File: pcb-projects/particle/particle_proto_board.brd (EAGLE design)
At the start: 94.6 x 65.7 mm, 35 parts, among them IC1 ATTINY20-MMH, IC2 DMC2400V, IC3 DMC2400V

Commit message: close 21, close 22
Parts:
- added SPI: 332-06, con-garry:332-06
- TPI: value 332-04 -> 332-06; device con-garry:332-04 -> con-garry:332-06
- moved TPI 84.6 mm to (-5.08, 6.35), turned to 0 degrees
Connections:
- removed net N$22: IC1.14, LED3.A, TP12.TP
- removed net N$23: IC1.15, LED2.A, TP11.TP
- removed net TPI_DATA: IC1.12, TPI.4
- new net MISO: IC1.14, LED3.A, SPI.1, TP12.TP
- new net SCK: IC1.15, LED2.A, SPI.3, TP11.TP
- new net TPI_DATA/MOSI: IC1.12, SPI.4, TPI.1
- net GND: now also SPI.6, TPI.4, TPI.6; no longer TPI.1
- net RESET: now also SPI.5, TPI.5; no longer TPI.3
- net TPI_CLK: now also TPI.3; no longer TPI.2
- net VCC: now also SPI.2, TPI.2
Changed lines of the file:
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@@
 </autorouter>
 <elements>
-<element name="TPI" library="con-garry" package="332-04" value="332-04" x="71.12" y="43.18" smashed="yes" rot="R90">
-<attribute name="NAME" x="70.835" y="37.75" size="1.27" layer="25" rot="R90"/>
-<attribute name="VALUE" x="67.58" y="41.56" size="1.27" layer="27" rot="R90"/>
-</element>
 <element name="IC1" library="tiny_particles_MCU" package="QFN45P300X300X85-21N" value="ATTINY20-MMH" x="63.1825" y="48.5775"/>
 <element name="R5" library="rcl" package="R1210" value="470" x="87.9475" y="56.1975"/>
@@
 <attribute name="TP_SIGNAL_NAME" value="" x="32.385" y="-16.8275" size="1.778" layer="27" display="off"/>
 </element>
+<element name="TPI" library="con-garry" package="332-06" value="332-06" x="-5.08" y="6.35"/>
+<element name="SPI" library="con-garry" package="332-06" value="332-06" x="-13.335" y="6.35"/>
 </elements>
 <signals>
 <signal name="GND">
-<contactref element="TPI" pad="1"/>
 <contactref element="IC1" pad="8"/>
 <contactref element="IC1" pad="21"/>
@@
 <contactref element="R6" pad="1"/>
 <contactref element="R9" pad="1"/>
-<wire x1="56.0675" y1="28.575" x2="56.9675" y2="4.23" width="0" layer="19" extent="1-1"/>
+<contactref element="TPI" pad="6"/>
+<contactref element="SPI" pad="6"/>
+<contactref element="TPI" pad="4"/>
+<wire x1="89.03" y1="52.07" x2="89.3475" y2="56.1975" width="0" layer="19" extent="1-1"/>
+<wire x1="89.03" y1="47.9425" x2="89.03" y2="52.07" width="0" layer="19" extent="1-1"/>
+<wire x1="63.1825" y1="48.5775" x2="89.03" y2="47.9425" width="0" layer="19" extent="1-1"/>
+<wire x1="63.1825" y1="47.1297" x2="63.1825" y2="48.5775" width="0" layer="19" extent="1-1"/>
+<wire x1="56.0675" y1="28.575" x2="63.1825" y2="47.1297" width="0" layer="19" extent="1-1"/>
 <wire x1="50.3525" y1="28.575" x2="56.0675" y2="28.575" width="0" layer="19" extent="1-1"/>
-<wire x1="3.68" y1="32.0675" x2="50.3525" y2="28.575" width="0" layer="19" extent="1-1"/>
-<wire x1="3.68" y1="45.4025" x2="3.68" y2="32.0675" width="0" layer="19" extent="1-1"/>
-<wire x1="36.6475" y1="54.0775" x2="3.68" y2="45.4025" width="0" layer="19" extent="1-1"/>
-<wire x1="63.1825" y1="47.1297" x2="36.6475" y2="54.0775" width="0" layer="19" extent="1-1"/>
-<wire x1="63.1825" y1="48.5775" x2="63.1825" y2="47.1297" width="0" layer="19" extent="1-1"/>
-<wire x1="72.12" y1="42.18" x2="63.1825" y2="47.1297" width="0" layer="19" extent="1-1"/>
-<wire x1="89.03" y1="47.9425" x2="72.12" y2="42.18" width="0" layer="19" extent="1-1"/>
-<wire x1="89.03" y1="52.07" x2="89.03" y2="47.9425" width="0" layer="19" extent="1-1"/>
-<wire x1="89.3475" y1="56.1975" x2="89.03" y2="52.07" width="0" layer="19" extent="1-1"/>
+<wire x1="56.9675" y1="4.23" x2="56.0675" y2="28.575" width="0" layer="19" extent="1-1"/>
+<wire x1="36.6475" y1="54.0775" x2="63.1825" y2="48.5775" width="0" layer="19" extent="1-1"/>
+<wire x1="3.68" y1="45.4025" x2="36.6475" y2="54.0775" width="0" layer="19" extent="1-1"/>
+<wire x1="3.68" y1="32.0675" x2="3.68" y2="45.4025" width="0" layer="19" extent="1-1"/>
+<wire x1="-3.08" y1="7.35" x2="3.68" y2="32.0675" width="0" layer="19" extent="1-1"/>
+<wire x1="-5.08" y1="7.35" x2="-3.08" y2="7.35" width="0" layer="19" extent="1-1"/>
+<wire x1="-11.335" y1="7.35" x2="-5.08" y2="7.35" width="0" layer="19" extent="1-1"/>
 </signal>
 <signal name="TPI_CLK">
-<contactref element="TPI" pad="2"/>
 <contactref element="IC1" pad="11"/>
-<wire x1="64.6303" y1="47.6885" x2="70.12" y2="42.18" width="0" layer="19" extent="1-1"/>
+<contactref element="TPI" pad="3"/>
+<wire x1="-5.08" y1="5.35" x2="64.6303" y2="47.6885" width="0" layer="19" extent="1-1"/>
 </signal>
 <signal name="PWR_TX_B">
@@
 <wire x1="61.7347" y1="48.1203" x2="37.1475" y2="54.0775" width="0" layer="19" extent="1-1"/>
 </signal>
-<signal name="TPI_DATA">
-<contactref element="TPI" pad="4"/>
+<signal name="TPI_DATA/MOSI">
 <contactref element="IC1" pad="12"/>
-<wire x1="64.6303" y1="48.1203" x2="70.12" y2="44.18" width="0" layer="19" extent="1-1"/>
+<contactref element="TPI" pad="1"/>
+<contactref element="SPI" pad="4"/>
+<wire x1="-7.08" y1="5.35" x2="64.6303" y2="48.1203" width="0" layer="19" extent="1-1"/>
+<wire x1="-13.335" y1="7.35" x2="-7.08" y2="5.35" width="0" layer="19" extent="1-1"/>
 </signal>
 <signal name="RESET">
-<contactref element="TPI" pad="3"/>
 <contactref element="IC1" pad="13"/>
-<wire x1="64.6303" y1="48.5775" x2="72.12" y2="44.18" width="0" layer="19" extent="1-1"/>
+<contactref element="TPI" pad="5"/>
+<contactref element="SPI" pad="5"/>
+<wire x1="-3.08" y1="5.35" x2="64.6303" y2="48.5775" width="0" layer="19" extent="1-1"/>
+<wire x1="-11.335" y1="5.35" x2="-3.08" y2="5.35" width="0" layer="19" extent="1-1"/>
 </signal>
 <signal name="RX_B" class="1">
@@
 <wire x1="64.0715" y1="50.0253" x2="71.4375" y2="54.9275" width="0" layer="19" extent="1-1"/>
 </signal>
-<signal name="N$22">
+<signal name="MISO">
 <contactref element="IC1" pad="14"/>
 <contactref element="LED3" pad="A"/>
 <contactref element="TP12" pad="TP"/>
+<contactref element="SPI" pad="1"/>
 <wire x1="71.12" y1="48.5775" x2="74.45" y2="49.2125" width="0" layer="19" extent="1-1"/>
 <wire x1="64.6303" y1="49.0347" x2="71.12" y2="48.5775" width="0" layer="19" extent="1-1"/>
-</signal>
-<signal name="N$23">
+<wire x1="-15.335" y1="5.35" x2="64.6303" y2="49.0347" width="0" layer="19" extent="1-1"/>
+</signal>
+<signal name="SCK">
 <contactref element="LED2" pad="A"/>
 <contactref element="TP11" pad="TP"/>
 <contactref element="IC1" pad="15"/>
+<contactref element="SPI" pad="3"/>
 <wire x1="71.4375" y1="51.7525" x2="74.45" y2="52.07" width="0" layer="19" extent="1-1"/>
 <wire x1="64.6303" y1="49.4665" x2="71.4375" y2="51.7525" width="0" layer="19" extent="1-1"/>
+<wire x1="-13.335" y1="5.35" x2="64.6303" y2="49.4665" width="0" layer="19" extent="1-1"/>
 </signal>
 <signal name="N$24">
@@
 <contactref element="IC3" pad="4"/>
 <contactref element="IC2" pad="4"/>
+<contactref element="TPI" pad="2"/>
+<contactref element="SPI" pad="2"/>
 <wire x1="47.4375" y1="28.575" x2="63.6397" y2="47.1297" width="0" layer="19" extent="1-1"/>
 <wire x1="57.9675" y1="5.93" x2="47.4375" y2="28.575" width="0" layer="19" extent="1-1"/>
 <wire x1="37.6475" y1="55.7775" x2="63.6397" y2="47.1297" width="0" layer="19" extent="1-1"/>
 <wire x1="17.275" y1="59.055" x2="37.6475" y2="55.7775" width="0" layer="19" extent="1-1"/>
+<wire x1="-7.08" y1="7.35" x2="17.275" y2="59.055" width="0" layer="19" extent="1-1"/>
+<wire x1="-15.335" y1="7.35" x2="-7.08" y2="7.35" width="0" layer="19" extent="1-1"/>
 </signal>
 <signal name="N$1">

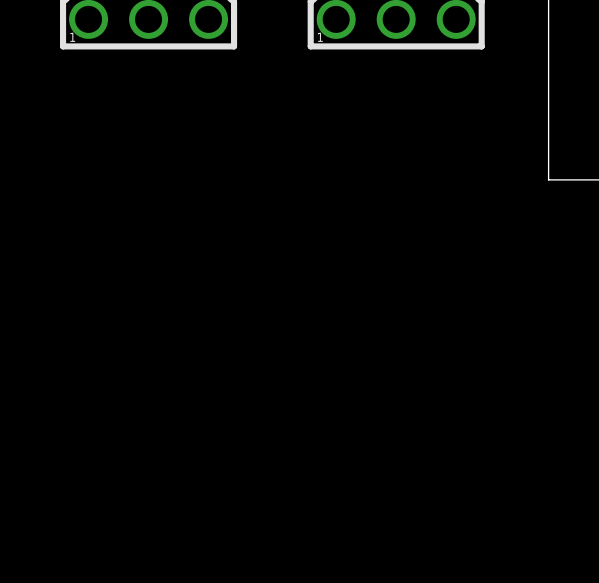
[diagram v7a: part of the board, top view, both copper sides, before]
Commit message: fixes #13
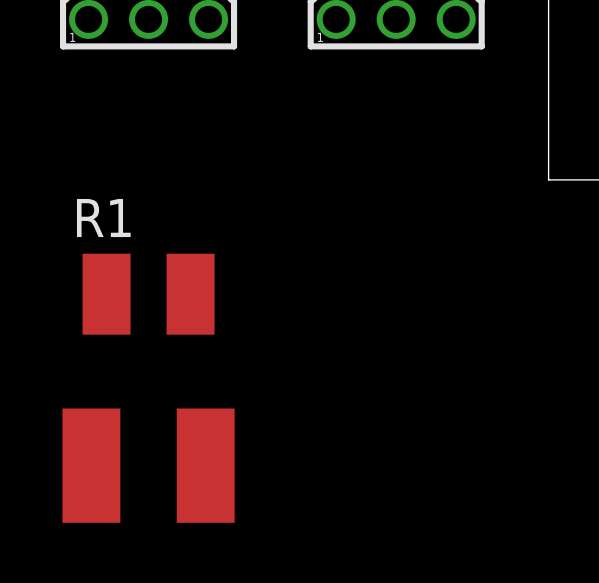
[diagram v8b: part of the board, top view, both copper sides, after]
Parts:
- added R1: 1k, rcl:R1210
- added RESET-SW: PAD-RESET-SWITCH, reset_pad:SWITCH-PAD-FORMED
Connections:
- net GND: now also RESET-SW.P$1
- net RESET: now also R1.1, RESET-SW.P$2
- net VCC: now also R1.2
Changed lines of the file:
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@@
 <layer number="54" name="bGND_GNDA" color="1" fill="9" visible="no" active="no"/>
 <layer number="56" name="wert" color="7" fill="1" visible="no" active="no"/>
+<layer number="90" name="Modules" color="5" fill="1" visible="no" active="no"/>
 <layer number="91" name="Nets" color="2" fill="1" visible="no" active="no"/>
 <layer number="92" name="Busses" color="1" fill="1" visible="no" active="no"/>
@@
 <element name="TPI" library="con-garry" package="332-06" value="332-06" x="-5.08" y="6.35"/>
 <element name="SPI" library="con-garry" package="332-06" value="332-06" x="-13.335" y="6.35"/>
+<element name="R1" library="rcl" package="R1210" value="1k" x="-13.335" y="-3.81"/>
+<element name="RESET-SW" library="reset_pad" package="SWITCH-PAD-FORMED" value="PAD-RESET-SWITCH" x="-13.97" y="-9.525"/>
 </elements>
 <signals>
@@
 <contactref element="SPI" pad="6"/>
 <contactref element="TPI" pad="4"/>
+<contactref element="RESET-SW" pad="P$1"/>
 <wire x1="89.03" y1="52.07" x2="89.3475" y2="56.1975" width="0" layer="19" extent="1-1"/>
 <wire x1="89.03" y1="47.9425" x2="89.03" y2="52.07" width="0" layer="19" extent="1-1"/>
@@
 <wire x1="-5.08" y1="7.35" x2="-3.08" y2="7.35" width="0" layer="19" extent="1-1"/>
 <wire x1="-11.335" y1="7.35" x2="-5.08" y2="7.35" width="0" layer="19" extent="1-1"/>
+<wire x1="-15.24" y1="-9.525" x2="-11.335" y2="7.35" width="0" layer="19" extent="1-1"/>
 </signal>
 <signal name="TPI_CLK">
@@
 <contactref element="TPI" pad="5"/>
 <contactref element="SPI" pad="5"/>
+<contactref element="R1" pad="1"/>
+<contactref element="RESET-SW" pad="P$2"/>
 <wire x1="-3.08" y1="5.35" x2="64.6303" y2="48.5775" width="0" layer="19" extent="1-1"/>
 <wire x1="-11.335" y1="5.35" x2="-3.08" y2="5.35" width="0" layer="19" extent="1-1"/>
+<wire x1="-14.735" y1="-3.81" x2="-11.335" y2="5.35" width="0" layer="19" extent="1-1"/>
+<wire x1="-11.43" y1="-9.525" x2="-14.735" y2="-3.81" width="0" layer="19" extent="1-1"/>
 </signal>
 <signal name="RX_B" class="1">
@@
 <contactref element="TPI" pad="2"/>
 <contactref element="SPI" pad="2"/>
+<contactref element="R1" pad="2"/>
 <wire x1="47.4375" y1="28.575" x2="63.6397" y2="47.1297" width="0" layer="19" extent="1-1"/>
 <wire x1="57.9675" y1="5.93" x2="47.4375" y2="28.575" width="0" layer="19" extent="1-1"/>
@@
 <wire x1="-7.08" y1="7.35" x2="17.275" y2="59.055" width="0" layer="19" extent="1-1"/>
 <wire x1="-15.335" y1="7.35" x2="-7.08" y2="7.35" width="0" layer="19" extent="1-1"/>
+<wire x1="-11.935" y1="-3.81" x2="-15.335" y2="7.35" width="0" layer="19" extent="1-1"/>
 </signal>
 <signal name="N$1">
